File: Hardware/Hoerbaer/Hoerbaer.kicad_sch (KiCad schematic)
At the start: 41 parts, among them J1 I2C, J11 UART, J13 JTAG, J17 RST_BOOT, J2 DISPLAY, J3 uSD, J4 USB1, J5 ENCODER, SW1 RESET, SW2 PROG, U1 ESP32 S3 MINI

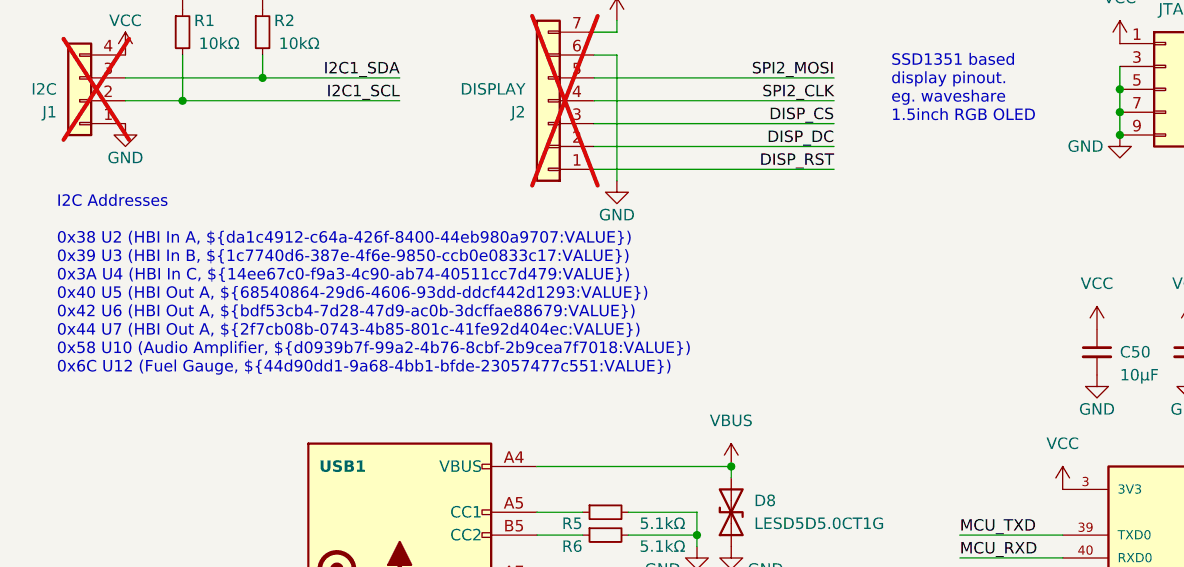
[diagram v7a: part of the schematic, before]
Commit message: Audio Progress... codec registers vs. I2S configuration.
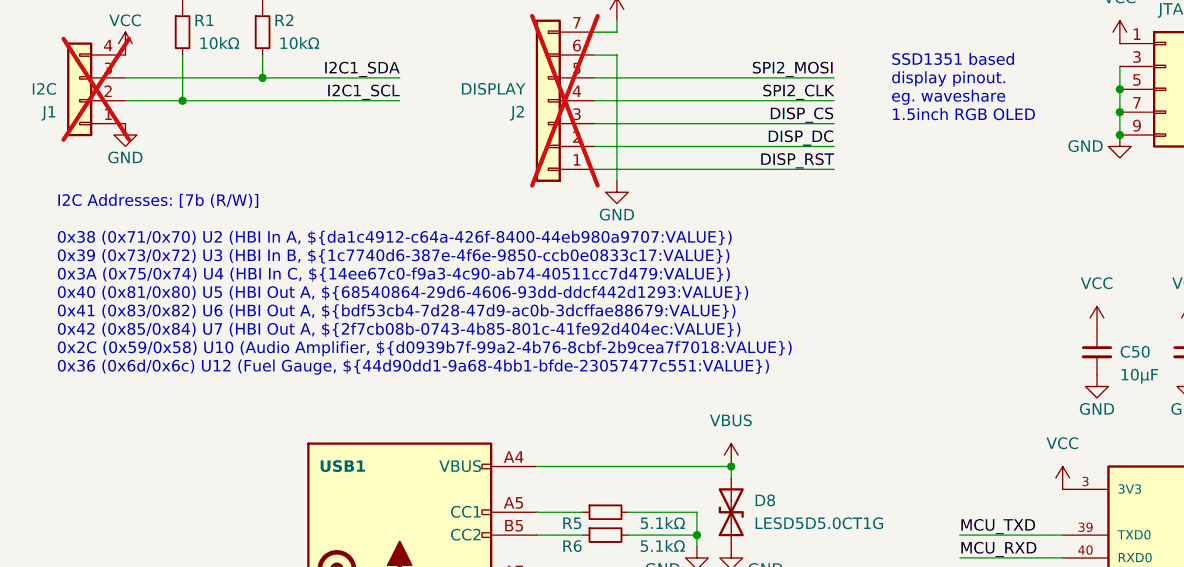
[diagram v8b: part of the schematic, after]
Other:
- note added: "I2C Addresses: [7b (R/W)] 0x38 (0x71/0x70) U2 (HBI In A, ${da1c4912-c64a-426f-8400-44eb980a9707:VALUE}) 0x39 (0x73/0x72) U3 (HBI In B, ${1c7740d6-387e-4f6e-9850-ccb0e0833c17:VALUE}) 0x3A (0x75/0x74) U4 (HBI In C, ${14ee67c0-f9a3-4c90-ab74-40511cc7d479:VALUE}) 0x40 (0x81/0x80) U5 (HBI Out A, ${68540864-29d6-4606-93dd-ddcf442d1293:VALUE}) 0x41 (0x83/0x82) U6 (HBI Out A, ${bdf53cb4-7d28-47d9-ac0b-3d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"
- note removed: "I2C Addresses 0x38 U2 (HBI In A, ${da1c4912-c64a-426f-8400-44eb980a9707:VALUE}) 0x39 U3 (HBI In B, ${1c7740d6-387e-4f6e-9850-ccb0e0833c17:VALUE}) 0x3A U4 (HBI In C, ${14ee67c0-f9a3-4c90-ab74-40511cc7d479:VALUE}) 0x40 U5 (HBI Out A, ${68540864-29d6-4606-93dd-ddcf442d1293:VALUE}) 0x42 U6 (HBI Out A, ${bdf53cb4-7d28-47d9-ac0b-3dcffae88679:VALUE}) 0x44 U7 (HBI Out A, ${2f7cb08b-0743-4b85-801c-41fe92d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"
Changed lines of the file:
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@@
     (effects (font (size 1.27 1.27)) (justify left bottom))
   )
-  (text "I2C Addresses\n\n0x38 U2 (HBI In A, ${da1c4912-c64a-426f-8400-44eb980a9707:VALUE})\n0x39 U3 (HBI In B, ${1c7740d6-387e-4f6e-9850-ccb0e0833c17:VALUE})\n0x3A U4 (HBI In C, ${14ee67c0-f9a3-4c90-ab74-40511cc7d479:VALUE})\n0x40 U5 (HBI Out A, ${68540864-29d6-4606-93dd-ddcf442d1293:VALUE})\n0x42 U6 (HBI Out A, ${bdf53cb4-7d28-47d9-ac0b-3dcffae88679:VALUE})\n0x44 U7 (HBI Out A, ${2f7cb08b-0743-4b85-801c-41fe92d404ec:VALUE})\n0x58 U10 (Audio Amplifier, ${d0939b7f-99a2-4b76-8cbf-2b9cea7f7018:VALUE})\n0x6C U12 (Fuel Gauge, ${44d90dd1-9a68-4bb1-bfde-23057477c551:VALUE})"
+  (text "I2C Addresses: [7b (R/W)]\n\n0x38 (0x71/0x70) U2 (HBI In A, ${da1c4912-c64a-426f-8400-44eb980a9707:VALUE})\n0x39 (0x73/0x72) U3 (HBI In B, ${1c7740d6-387e-4f6e-9850-ccb0e0833c17:VALUE})\n0x3A (0x75/0x74) U4 (HBI In C, ${14ee67c0-f9a3-4c90-ab74-40511cc7d479:VALUE})\n0x40 (0x81/0x80) U5 (HBI Out A, ${68540864-29d6-4606-93dd-ddcf442d1293:VALUE})\n0x41 (0x83/0x82) U6 (HBI Out A, ${bdf53cb4-7d28-47d9-ac0b-3dcffae88679:VALUE})\n0x42 (0x85/0x84) U7 (HBI Out A, ${2f7cb08b-0743-4b85-801c-41fe92d404ec:VALUE})\n0x2C (0x59/0x58) U10 (Audio Amplifier, ${d0939b7f-99a2-4b76-8cbf-2b9cea7f7018:VALUE})\n0x36 (0x6d/0x6c) U12 (Fuel Gauge, ${44d90dd1-9a68-4bb1-bfde-23057477c551:VALUE})"
     (at 27.94 63.5 0)
     (effects (font (size 1.27 1.27)) (justify left bottom))
